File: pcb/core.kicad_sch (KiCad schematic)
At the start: 44 parts, among them J201 Debug, J202 Computer, J203 Power, J204 Device, Q201 USB Power Switch, U201 16Mb NOR Flash, U202 3V3 250ma LDO Regulator, U203 Microcontroller, X201 12MHz CMOS Oscillator

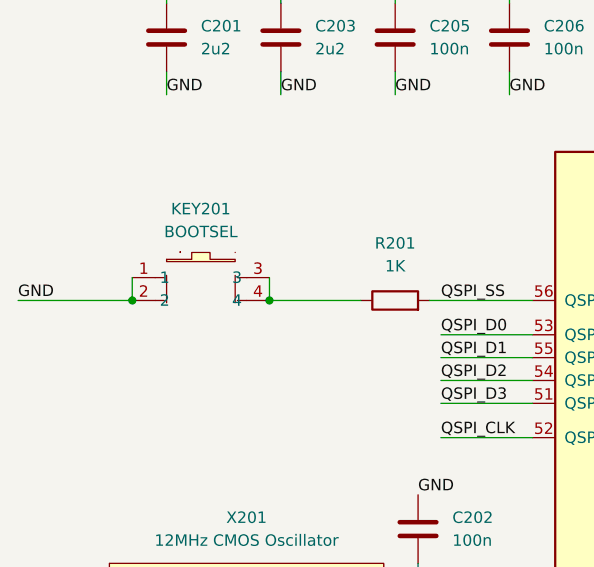
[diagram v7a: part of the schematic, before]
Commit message: Switch to a smaller pushbutton (similar to the one on the Pico)
Edit imported symbols to use 'LCSC' instead of 'LCSC Part' field name
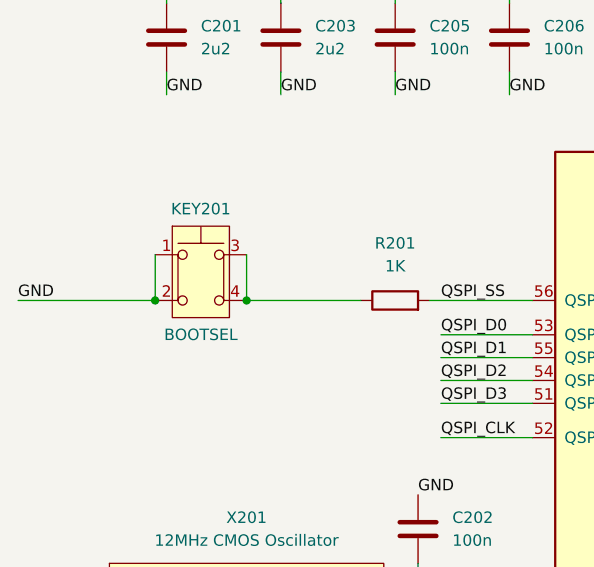
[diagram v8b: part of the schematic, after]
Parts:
- KEY201: footprint LCSC_C86487:KEY-SMD_4P-L6.0-W6.0-P4.50 -> LCSC_C470427:KEY-SMD_4P-L4.2-W3.2-P2.20-LS4.6; symbol LCSC_C86487:4-1437565-2 -> LCSC_C470427:SKRPASE010; LCSC C86487 -> C470427; MPN 4-1437565-2 -> SKRPASE010
- U203: footprint RP2040_minimal_r2:RP2040-QFN-56 -> RP2040_minimal:RP2040-QFN-56
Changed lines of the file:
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@@
   (junction (at 242.57 19.05) (diameter 0) (color 0 0 0 0)
   )
-  (junction (at 26.67 58.42) (diameter 0) (color 0 0 0 0)
-  )
   (junction (at 265.43 50.8) (diameter 0) (color 0 0 0 0)
   )
+  (junction (at 39.37 58.42) (diameter 0) (color 0 0 0 0)
+  )
   (junction (at 267.97 146.05) (diameter 0) (color 0 0 0 0)
   )
   (junction (at 93.98 38.1) (diameter 0) (color 0 0 0 0)
   )
-  (junction (at 41.91 58.42) (diameter 0) (color 0 0 0 0)
-  )
   (junction (at 33.02 182.88) (diameter 0) (color 0 0 0 0)
   )
@@
   )
   (junction (at 267.97 116.84) (diameter 0) (color 0 0 0 0)
+  )
+  (junction (at 29.21 58.42) (diameter 0) (color 0 0 0 0)
   )
   (no_connect (at 255.27 92.71))
@@
     (stroke (width 0) (type default))
   )
+  (wire (pts (xy 39.37 53.34) (xy 39.37 58.42))
+    (stroke (width 0) (type default))
+  )
   (wire (pts (xy 58.42 87.63) (xy 58.42 90.17))
     (stroke (width 0) (type default))
@@
     (stroke (width 0) (type default))
   )
+  (wire (pts (xy 29.21 53.34) (xy 29.21 58.42))
+    (stroke (width 0) (type default))
+  )
   (wire (pts (xy 134.62 87.63) (xy 158.75 87.63))
     (stroke (width 0) (type default))
@@
     (stroke (width 0) (type default))
   )
-  (wire (pts (xy 41.91 58.42) (xy 52.07 58.42))
+  (wire (pts (xy 39.37 58.42) (xy 52.07 58.42))
     (stroke (width 0) (type default))
   )
@@
     (stroke (width 0) (type default))
   )
-  (wire (pts (xy 13.97 58.42) (xy 26.67 58.42))
+  (wire (pts (xy 13.97 58.42) (xy 29.21 58.42))
     (stroke (width 0) (type default))
   )
@@
     (stroke (width 0) (type default))
   )
-  (wire (pts (xy 26.67 55.88) (xy 26.67 58.42))
-    (stroke (width 0) (type default))
-  )
   (wire (pts (xy 55.88 140.97) (xy 58.42 140.97))
     (stroke (width 0) (type default))
@@
   )
   (wire (pts (xy 134.62 102.87) (xy 138.43 102.87))
-    (stroke (width 0) (type default))
-  )
-  (wire (pts (xy 41.91 55.88) (xy 41.91 58.42))
     (stroke (width 0) (type default))
   )
@@
     )
   )
-  (symbol (lib_id "LCSC_C86487:4-1437565-2") (at 34.29 55.88 0) (unit 1)
-    (in_bom yes) (on_board yes) (dnp no) (fields_autoplaced)
+  (symbol (lib_id "LCSC_C470427:SKRPASE010") (at 34.29 55.88 0) (unit 1)
+    (in_bom yes) (on_board yes) (dnp no)
     (property "Reference" "KEY201" (at 34.29 48.26 0)
       (effects (font (size 1.27 1.27)))
     )
-    (property "Value" "BOOTSEL" (at 34.29 50.8 0)
+    (property "Value" "BOOTSEL" (at 34.29 62.23 0)
       (effects (font (size 1.27 1.27)))
     )
-    (property "Footprint" "LCSC_C86487:KEY-SMD_4P-L6.0-W6.0-P4.50" (at 34.29 66.04 0)
-      (effects (font (size 1.27 1.27)) hide)
-    )
-    (property "Datasheet" "https://lcsc.com/product-detail/Tactile-Switches_TE-Connectivity_4-1437565-2_6-6-5-0-25mm-Operational-force160gf_C86487.html" (at 34.29 68.58 0)
-      (effects (font (size 1.27 1.27)) hide)
-    )
-    (property "LCSC" "C86487" (at 34.29 71.12 0)
-      (effects (font (size 1.27 1.27)) hide)
-    )
-    (property "MPN" "4-1437565-2" (at 34.29 55.88 0)
+    (property "Footprint" "LCSC_C470427:KEY-SMD_4P-L4.2-W3.2-P2.20-LS4.6" (at 34.29 66.04 0)
+      (effects (font (size 1.27 1.27)) hide)
+    )
+    (property "Datasheet" "https://lcsc.com/product-detail/Tactile-Switches_ALPS-Electric-SKRPASE010_C470427.html" (at 34.29 68.58 0)
+      (effects (font (size 1.27 1.27)) hide)
+    )
+    (property "LCSC" "C470427" (at 34.29 71.12 0)
+      (effects (font (size 1.27 1.27)) hide)
+    )
+    (property "MPN" "SKRPASE010" (at 34.29 55.88 0)
       (effects (font (size 1.27 1.27)) hide)
     )
@@
       (effects (font (size 1.27 1.27)) (justify left))
     )
-    (property "Footprint" "RP2040_minimal_r2:RP2040-QFN-56" (at 83.82 90.17 0)
-      (effects (font (size 1.27 1.27)) hide)
-    )
+    (property "Footprint" "RP2040_minimal:RP2040-QFN-56" (at 83.82 90.17 0)
+      (effects (font (size 1.27 1.27)) hide)
+    )
